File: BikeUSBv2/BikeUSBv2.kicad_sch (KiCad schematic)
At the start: 48 parts, among them J1 TYPE-C-31-M-16, J2 Conn_01x02_Female, Q1 SSM3J332R,LF, Q2 SSM3J332R,LF, SW1 SW_Push, SW2 SW_Push, U1 TPS63020DSJR, U2 ATtiny1616-M

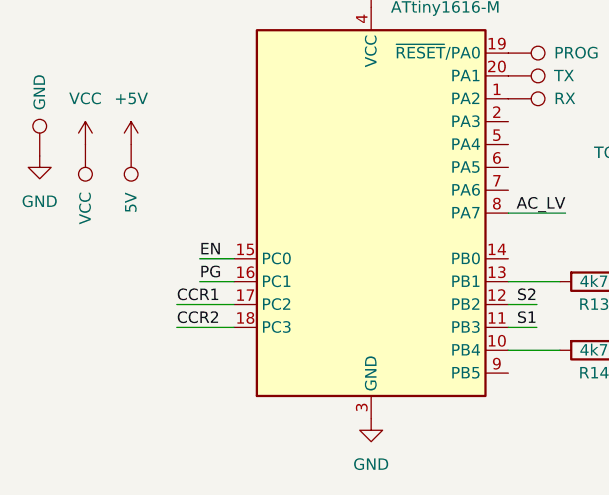
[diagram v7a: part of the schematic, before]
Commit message: fix clearances, routing almost done
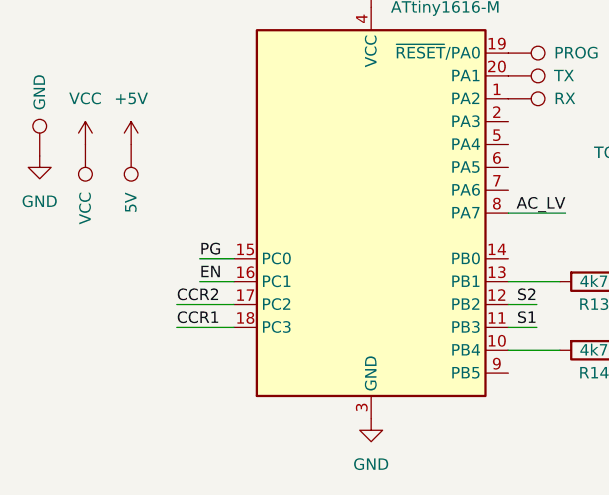
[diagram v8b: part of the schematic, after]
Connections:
- net CCR1: now also U2.18 (PC3); no longer U2.17 (PC2)
- net CCR2: now also U2.17 (PC2); no longer U2.18 (PC3)
- net EN: now also U2.16 (PC1); no longer U2.15 (PC0)
- net PG: now also U2.15 (PC0); no longer U2.16 (PC1)
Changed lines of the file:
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@@
     (effects (font (size 1.27 1.27)) (justify right bottom))
   )
-  (label "CCR1" (at 34.29 173.99 0) (fields_autoplaced)
+  (label "CCR2" (at 34.29 173.99 0) (fields_autoplaced)
     (effects (font (size 1.27 1.27)) (justify left bottom))
   )
@@
     (effects (font (size 1.27 1.27)) (justify left bottom))
   )
-  (label "PG" (at 36.83 171.45 0) (fields_autoplaced)
+  (label "EN" (at 36.83 171.45 0) (fields_autoplaced)
     (effects (font (size 1.27 1.27)) (justify left bottom))
   )
@@
     (effects (font (size 1.27 1.27)) (justify left bottom))
   )
-  (label "EN" (at 36.83 168.91 0) (fields_autoplaced)
+  (label "PG" (at 36.83 168.91 0) (fields_autoplaced)
     (effects (font (size 1.27 1.27)) (justify left bottom))
   )
-  (label "CCR2" (at 34.29 176.53 0) (fields_autoplaced)
+  (label "CCR1" (at 34.29 176.53 0) (fields_autoplaced)
     (effects (font (size 1.27 1.27)) (justify left bottom))
   )
